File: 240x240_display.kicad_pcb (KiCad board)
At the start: 2 copper layers, 8 parts, among them J1 Conn_02x12_Counter_Clockwise, J5 Conn_01x09_Male, Q1 BSS138

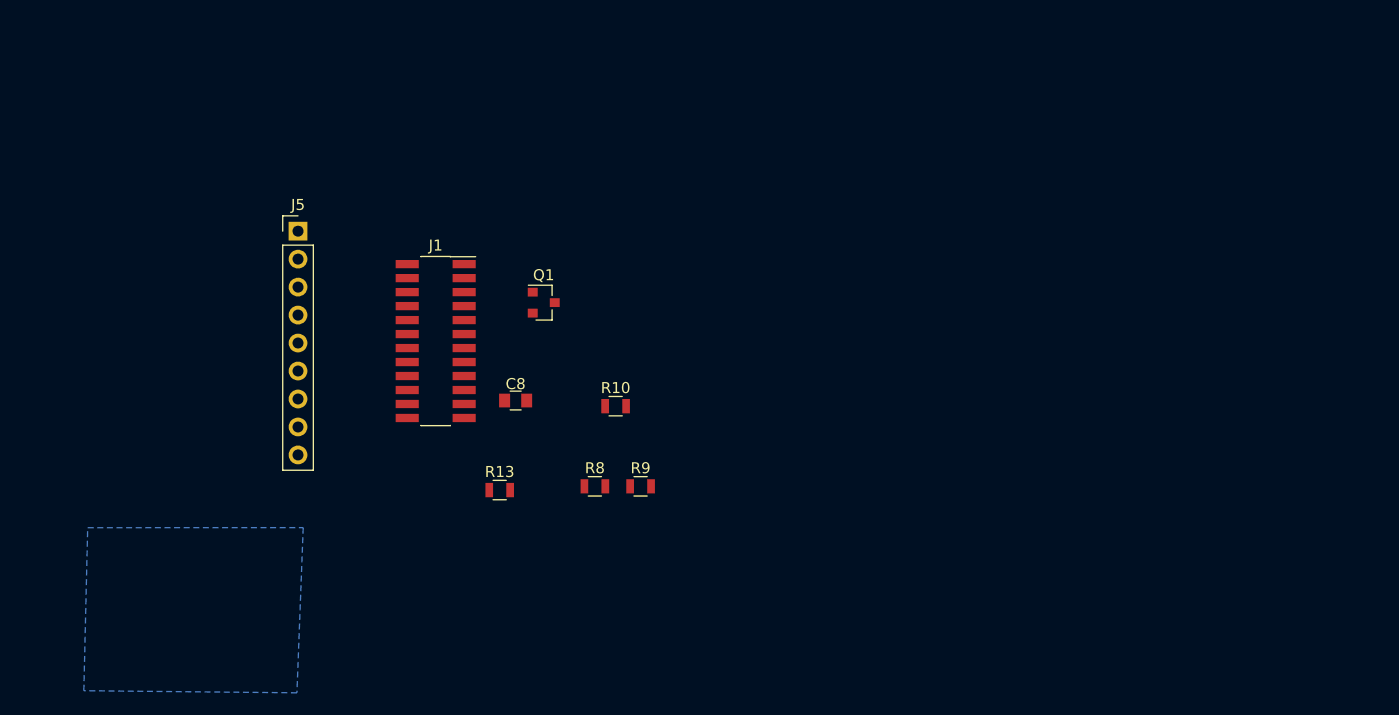
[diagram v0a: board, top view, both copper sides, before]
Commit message: update for display footprint
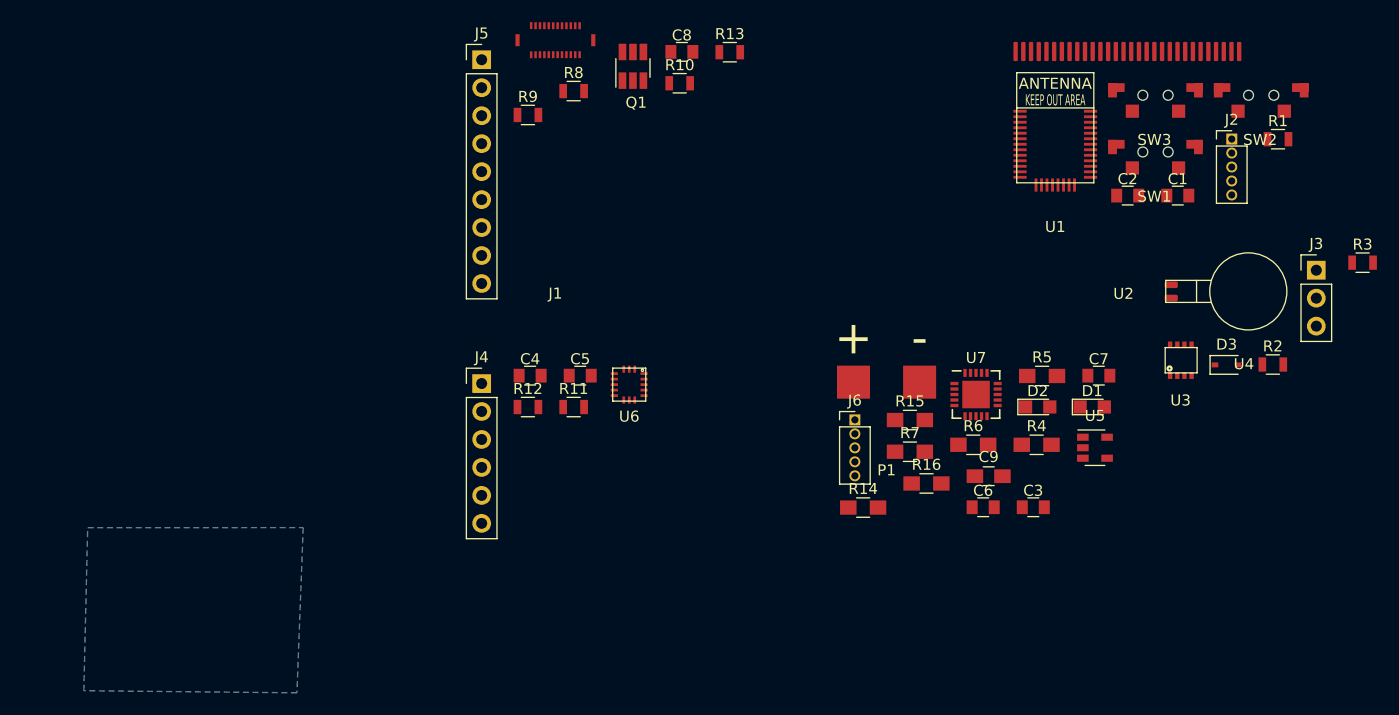
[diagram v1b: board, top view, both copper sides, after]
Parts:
- added C1: C, Capacitors_SMD:C_0805, F.Cu at (216.9, 76.6)
- added C2: C, Capacitors_SMD:C_0805, F.Cu at (212.3, 76.6)
- added C3: 470pF, Capacitors_SMD:C_0805, F.Cu at (203.7, 104.9)
- added C4: 100nF, Capacitors_SMD:C_0805, F.Cu at (158.1, 93.0)
- added C5: 10uF, Capacitors_SMD:C_0805, F.Cu at (162.6, 93.0)
- added C6: 470pF, Capacitors_SMD:C_0805, F.Cu at (199.2, 104.9)
- added C7: 470pF, Capacitors_SMD:C_0805, F.Cu at (209.7, 93.0)
- added C9: 10uF, Capacitors_SMD:C_0805_HandSoldering, F.Cu at (199.7, 102.1)
- added D1: ORANGE, LEDs:LED_0805, F.Cu at (209.1, 95.8)
- added D2: GREEN, LEDs:LED_0805, F.Cu at (204.1, 95.8)
- added D3: ZLLS410, Diodes_SMD:D_SOD-323, F.Cu at (221.3, 92.0)
- added J2: Conn_01x05, Pin_Headers:Pin_Header_Straight_1x05_Pitch1.27mm, F.Cu at (221.8, 71.5)
- added J3: Conn_01x03, Pin_Headers:Pin_Header_Straight_1x03_Pitch2.54mm, F.Cu at (229.4, 83.4)
- added J4: Conn_01x06, Pin_Headers:Pin_Header_Straight_1x06_Pitch2.54mm, F.Cu at (153.7, 93.7)
- added J6: CONN_01X05, Pin_Headers:Pin_Header_Straight_1x05_Pitch1.27mm, F.Cu at (187.5, 97.0)
- added P1: BATT, my-fp-library:Battery Pads 3x3, F.Cu at (190.4, 93.6)
- added R1: R, Resistors_SMD:R_0805, F.Cu at (226.0, 71.5)
- added R11: 10K, Resistors_SMD:R_0805, F.Cu at (162.0, 95.8)
- added R12: 10K, Resistors_SMD:R_0805, F.Cu at (157.9, 95.8)
- added R14: 100K, Resistors_SMD:R_0805_HandSoldering, F.Cu at (188.3, 105.0)
- added R15: 1K, Resistors_SMD:R_0805_HandSoldering, F.Cu at (192.5, 97.0)
- added R16: 10K, Resistors_SMD:R_0805_HandSoldering, F.Cu at (194.0, 102.8)
- added R2: 10K, Resistors_SMD:R_0805, F.Cu at (225.5, 92.0)
- added R3: 330, Resistors_SMD:R_0805, F.Cu at (233.6, 82.7)
- added R4: 1K, Resistors_SMD:R_0805_HandSoldering, F.Cu at (204.0, 99.3)
- added R5: 1K, Resistors_SMD:R_0805_HandSoldering, F.Cu at (204.5, 93.0)
- added R6: 270K, Resistors_SMD:R_0805_HandSoldering, F.Cu at (198.3, 99.3)
- added R7: 100K, Resistors_SMD:R_0805_HandSoldering, F.Cu at (192.5, 99.9)
- added SW1: UP, my-fp-library:Tact_SW_3x6x3.5, F.Cu at (214.8, 72.7)
- added SW2: MID, my-fp-library:Tact_SW_3x6x3.5, F.Cu at (224.4, 67.5)
- added SW3: DWN, my-fp-library:Tact_SW_3x6x3.5, F.Cu at (214.8, 67.5)
- added U1: BLYST-NRF52832-NANO, my-fp-library:BLYST NRF52832-NANO, F.Cu at (205.7, 70.5)
- added U2: Oled_128x64_SSD1306, my-fp-library:oled ssd1306 29x0.7mm, F.Cu at (211.9, 63.5)
- added U3: ECH8693R-TL-W, my-fp-library:SOT-28FL, F.Cu at (217.1, 91.5)
- added U4: C0720B001F, my-fp-library:VIBRATION MOTOR COIN 3V FLEX - C0720B001F, F.Cu at (223.3, 85.3)
- added U5: MIC5219-3.3YM5, TO_SOT_Packages_SMD:SOT-23-5, F.Cu at (209.3, 99.5)
- added U6: LIS3DH, my-fp-library:LGA-16_3x3mm, F.Cu at (167.1, 93.8)
- added U7: MCP73871-xxI_ML, Housings_DFN_QFN:QFN-20-1EP_4x4mm_Pitch0.5mm, F.Cu at (198.5, 94.7)
- J1: footprint Socket_Strips:Socket_Strip_Straight_2x12_Pitch1.27mm_SMD -> SMD_Packages:DF37B-24DP-0.4V(51)
- Q1: value BSS138 -> FDC6420C; footprint TO_SOT_Packages_SMD:SOT-23 -> TO_SOT_Packages_SMD:SuperSOT-6
- moved R13 44.9 mm to (176.2, 63.6)
- moved R8 35.9 mm to (162.0, 67.1)
- moved R9 35.2 mm to (157.9, 69.3)
- moved C8 35.1 mm to (171.8, 63.6)
- moved R10 29.9 mm to (171.6, 66.4)
- moved J1 29.4 mm to (160.3, 62.5)
- moved Q1 23.0 mm to (167.4, 64.9)
- moved J5 22.8 mm to (153.7, 64.3)
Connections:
- J5 pad 2: TEAR -> (no net)
- J5 pad 3: MOSI -> (no net)
- J5 pad 4: DC -> (no net)
- J5 pad 5: SCK -> (no net)
- Q1 pad 2: (GND) -> (no net)
- Q1 pad 3: Net-(Q1-Pad3) -> (no net)
- R9 pad 1: /240x240_display/LEDK -> (no net)
- R9 pad 2: Net-(Q1-Pad3) -> Net-(Q1-Pad6)

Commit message: update for power footprint
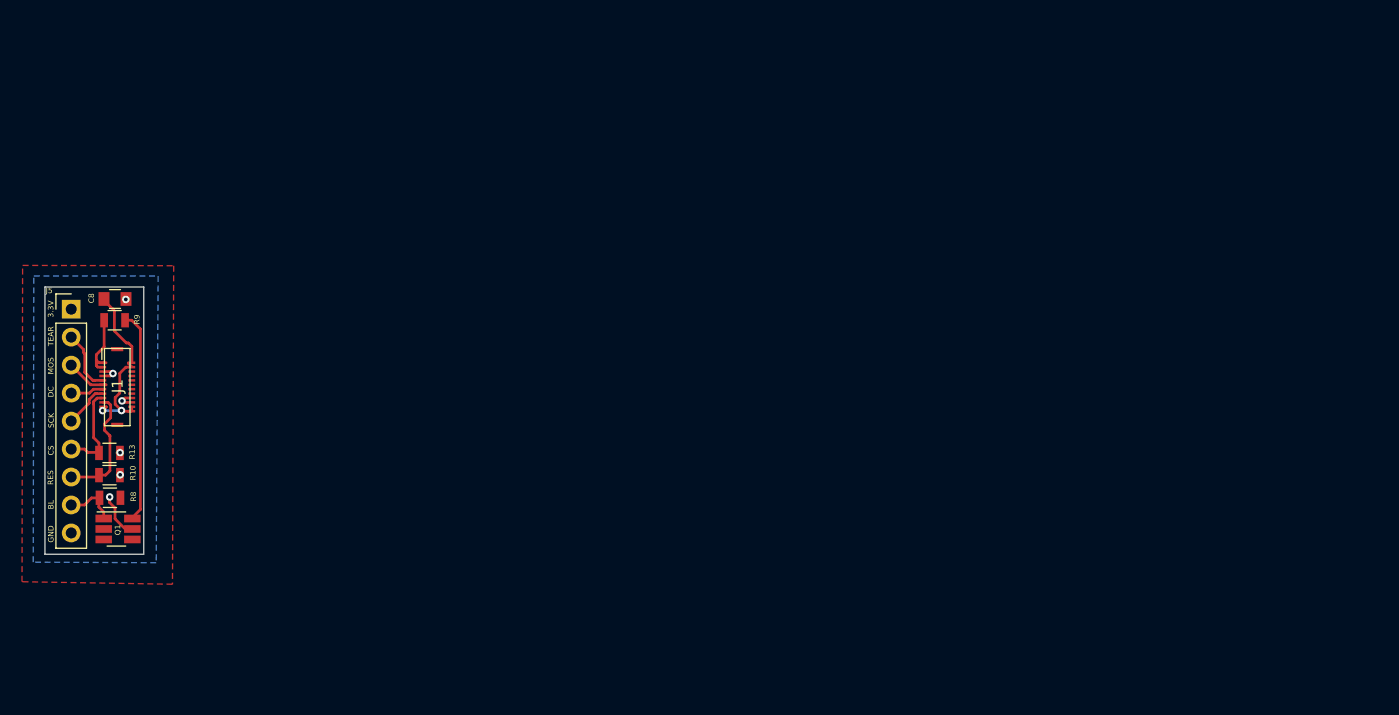
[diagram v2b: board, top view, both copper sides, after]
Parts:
- removed C1, C2: C, Capacitors_SMD:C_0805
- removed C3, C6, C7: 470pF, Capacitors_SMD:C_0805
- removed C4: 100nF, Capacitors_SMD:C_0805
- removed C5: 10uF, Capacitors_SMD:C_0805
- removed C9: 10uF, Capacitors_SMD:C_0805_HandSoldering
- removed D1: ORANGE, LEDs:LED_0805
- removed D2: GREEN, LEDs:LED_0805
- removed D3: ZLLS410, Diodes_SMD:D_SOD-323
- removed J2: Conn_01x05, Pin_Headers:Pin_Header_Straight_1x05_Pitch1.27mm
- removed J3: Conn_01x03, Pin_Headers:Pin_Header_Straight_1x03_Pitch2.54mm
- removed J4: Conn_01x06, Pin_Headers:Pin_Header_Straight_1x06_Pitch2.54mm
- removed J6: CONN_01X05, Pin_Headers:Pin_Header_Straight_1x05_Pitch1.27mm
- removed P1: BATT, my-fp-library:Battery Pads 3x3
- removed R1: R, Resistors_SMD:R_0805
- removed R11, R12, R2: 10K, Resistors_SMD:R_0805
- removed R14, R7: 100K, Resistors_SMD:R_0805_HandSoldering
- removed R15, R4, R5: 1K, Resistors_SMD:R_0805_HandSoldering
- removed R16: 10K, Resistors_SMD:R_0805_HandSoldering
- removed R3: 330, Resistors_SMD:R_0805
- removed R6: 270K, Resistors_SMD:R_0805_HandSoldering
- removed SW1: UP, my-fp-library:Tact_SW_3x6x3.5
- removed SW2: MID, my-fp-library:Tact_SW_3x6x3.5
- removed SW3: DWN, my-fp-library:Tact_SW_3x6x3.5
- removed U1: BLYST-NRF52832-NANO, my-fp-library:BLYST NRF52832-NANO
- removed U2: Oled_128x64_SSD1306, my-fp-library:oled ssd1306 29x0.7mm
- removed U3: ECH8693R-TL-W, my-fp-library:SOT-28FL
- removed U4: C0720B001F, my-fp-library:VIBRATION MOTOR COIN 3V FLEX - C0720B001F
- removed U5: MIC5219-3.3YM5, TO_SOT_Packages_SMD:SOT-23-5
- removed U6: LIS3DH, my-fp-library:LGA-16_3x3mm
- removed U7: MCP73871-xxI_ML, Housings_DFN_QFN:QFN-20-1EP_4x4mm_Pitch0.5mm
- moved R13 67.1 mm to (119.9, 100.0)
- moved Q1 62.9 mm to (120.6, 107.0), turned to 270 degrees
- moved R10 62.8 mm to (119.9, 102.0)
- moved C8 56.2 mm to (120.4, 86.0)
- moved R8 56.0 mm to (119.9, 104.1), turned to 180 degrees
- moved J1 50.7 mm to (120.6, 94.0), turned to 270 degrees
- moved J5 43.6 mm to (116.4, 86.9)
- moved R9 41.9 mm to (120.3, 88.0)
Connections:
- J5 pad 2: (no net) -> TEAR
- J5 pad 3: (no net) -> MOSI
- J5 pad 4: (no net) -> DC
- J5 pad 5: (no net) -> SCK
- R9 pad 1: (no net) -> /240x240_display/LEDK
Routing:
- net Net-(Q1-Pad6): track 0.00 -> 19.1 mm
- net +3.3: track 0.00 -> 15.7 mm, vias 0 -> 2
- net RESET: track 0.00 -> 10.9 mm
- net CS: track 0.00 -> 8.34 mm
- net (GND): track 0.00 -> 7.13 mm, vias 0 -> 6
- net /240x240_display/LEDK: track 0.00 -> 6.31 mm
- net TEAR: track 0.00 -> 5.66 mm
- net BACKLIGHT: track 0.00 -> 4.88 mm
- net SCK: track 0.00 -> 4.05 mm
- net MOSI: track 0.00 -> 3.92 mm
- net DC: track 0.00 -> 3.10 mm
- added copper zone on F.Cu, net +3.3
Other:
- board outline added: 9 x 24.3 mm
- net class Default: clearance 0.2 -> 0.1524
- rule pad_to_mask_clearance: 0.051 -> 0.0508
- rule solder_mask_min_width: 0.25 -> 0.101
- rule trace_clearance: 0.2 -> 0.1524
- rule trace_min: 0.2 -> 0.1524
- rule via_min_drill: 0.3 -> 0.254
- rule via_min_size: 0.4 -> 0.508
- board text added: "3.3V"
- board text added: "BL"
- board text added: "CS"
- board text added: "DC"
- board text added: "GND"
- board text added: "MOS"
- board text added: "RES"
- board text added: "SCK"
- board text added: "TEAR"

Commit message: Layout board
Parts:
- removed J5: Conn_01x09_Male, Pin_Headers:Pin_Header_Straight_1x09_Pitch2.54mm
- added C11: 1uF, Capacitors_SMD:C_0603_HandSoldering, F.Cu at (158.9, 72.8)
- added C2: 1uF, Capacitors_SMD:C_0603_HandSoldering, F.Cu at (159.0, 80.9)
- added J7: Conn_01x12, my-fp-library:FPC_12x0.7mm, B.Cu at (155.0, 90.5)
- added Q3: SI3139K, TO_SOT_Packages_SMD:SOT-723_Handsoldering, F.Cu at (152.9, 71.9)
- added Q4: SI3139K, TO_SOT_Packages_SMD:SOT-723_Handsoldering, F.Cu at (152.8, 76.2)
- added R18: 10K, Resistors_SMD:R_0603_HandSoldering, F.Cu at (152.7, 83.2)
- added R19: 10K, Resistors_SMD:R_0603_HandSoldering, F.Cu at (152.2, 96.3)
- added R2: 100K, Resistors_SMD:R_0603_HandSoldering, F.Cu at (155.6, 80.8)
- added R3: 2.2K, Resistors_SMD:R_0603_HandSoldering, F.Cu at (157.4, 80.8)
- C8: footprint Capacitors_SMD:C_0805 -> Capacitors_SMD:C_0603_HandSoldering
- J1: value Conn_02x12_Counter_Clockwise -> Conn_01x10; footprint SMD_Packages:DF37B-24DP-0.4V(51) -> Pin_Headers:Pin_Header_Straight_1x10_Pitch2.54mm
- Q1: value FDC6420C -> SI3139K; footprint TO_SOT_Packages_SMD:SuperSOT-6 -> TO_SOT_Packages_SMD:SOT-723_Handsoldering
- R10: value 10K -> 30; footprint Resistors_SMD:R_0805 -> Resistors_SMD:R_0603_HandSoldering
- R13: value 10K -> 100; footprint Resistors_SMD:R_0805 -> Resistors_SMD:R_0603_HandSoldering
- R8: value 2.2K -> 100K; footprint Resistors_SMD:R_0805 -> Resistors_SMD:R_0603_HandSoldering
- R9: value 10 -> 100K; footprint Resistors_SMD:R_0805 -> Resistors_SMD:R_0603_HandSoldering
- moved R10 47.7 mm to (157.4, 72.6), turned to 90 degrees
- moved R8 47.5 mm to (155.6, 72.6), turned to 90 degrees
- moved R13 44.2 mm to (157.4, 76.7), turned to 90 degrees
- moved Q1 41.8 mm to (152.8, 80.2), turned to 0 degrees
- moved R9 37.0 mm to (155.6, 76.7), turned to 90 degrees
- moved J1 34.9 mm to (148.3, 72.8), turned to 0 degrees
- moved C8 32.2 mm to (148.5, 70.5)
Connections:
- J1 pad 1: /240x240_display/LEDK -> /LIGHT1
- J1 pad 10: RESET -> (GND)
- J1 pad 2: /240x240_display/LEDK -> /LIGHT2
- J1 pad 3: (GND) -> /LIGHT3
- J1 pad 4: (GND) -> /SPI_DC
- J1 pad 5: TEAR -> /SPI_CS
- J1 pad 6: MOSI -> /SPI_SCK
- J1 pad 7: DC -> /SPI_MOSI
- J1 pad 8: SCK -> /SPI_RESET
- J1 pad 9: CS -> +3.3
- Q1 pad 1: BACKLIGHT -> /LIGHT3
- Q1 pad 2: (no net) -> +3.3
- Q1 pad 3: (no net) -> Net-(Q1-Pad3)
- R10 pad 1: RESET -> /LEDK
- R10 pad 2: (GND) -> Net-(Q3-Pad3)
- R13 pad 1: CS -> /LEDK
- R13 pad 2: (GND) -> Net-(Q4-Pad3)
- R8 pad 2: BACKLIGHT -> /LIGHT1
- R9 pad 1: /240x240_display/LEDK -> +3.3
- R9 pad 2: Net-(Q1-Pad6) -> /LIGHT2
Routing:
- net /SPI_CS: track 0.00 -> 30.7 mm, vias 0 -> 1
- net Net-(Q1-Pad6): track 19.1 -> 0.00 mm
- net /SPI_RESET: track 0.00 -> 17.4 mm, vias 0 -> 2
- net /LEDK: track 0.00 -> 16.7 mm, vias 0 -> 1
- net /SPI_DC: track 0.00 -> 14.2 mm, vias 0 -> 1
- net RESET: track 10.9 -> 0.00 mm
- net /SPI_SCK: track 0.00 -> 10.7 mm, vias 0 -> 1
- net /LIGHT3: track 0.00 -> 8.98 mm
- net +3.3: track 15.7 -> 6.81 mm, vias 2 -> 1
- net /SPI_MOSI: track 0.00 -> 8.87 mm, vias 0 -> 1
- net /LIGHT2: track 0.00 -> 8.60 mm
- net CS: track 8.34 -> 0.00 mm
- net /LIGHT1: track 0.00 -> 7.99 mm
- net (GND): track 7.13 -> 13.5 mm, vias 6 -> 5
- net /240x240_display/LEDK: track 6.31 -> 0.00 mm
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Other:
- board size 9 x 24.3 mm -> 14 x 28 mm
- board text added: "+3.3"
- board text added: "L1"
- board text added: "L2"
- board text added: "L3"
- board text added: "RST"
- board text removed: "3.3V"
- board text removed: "BL"
- board text removed: "RES"
- board text removed: "TEAR"

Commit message: More layout changes
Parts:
- added R5: 1, Resistors_SMD:R_0603_HandSoldering, F.Cu at (157.1, 86.2)
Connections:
- J7 pad 2: /LEDK -> Net-(J7-Pad2)
- J7 pad 3: +3.3 -> /LEDA
- R10 pad 1: /LEDK -> /LEDA
- R13 pad 1: /LEDK -> /LEDA
- R3 pad 1: /LEDK -> /LEDA
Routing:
- net /LEDA: track 0.00 -> 19.6 mm, vias 0 -> 2
- net /LEDK: track 16.7 -> 0.00 mm, vias 1 -> 0
- net Net-(J7-Pad2): track 0.00 -> 2.05 mm, vias 0 -> 1
- net (GND): track 13.5 -> 14.8 mm, vias 5 -> 6
